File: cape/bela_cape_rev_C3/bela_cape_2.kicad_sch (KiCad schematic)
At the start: 18 parts, among them IC7 TSV524xIQ4T, IC8 TSV524xIQ4T, IC9 ADS8168

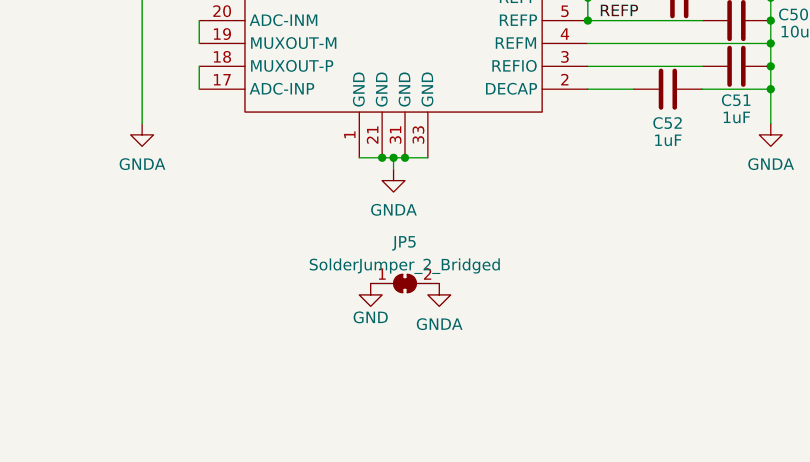
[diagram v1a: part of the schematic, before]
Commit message: removed sym-lib-table with a reference to an unused and obsolete local library
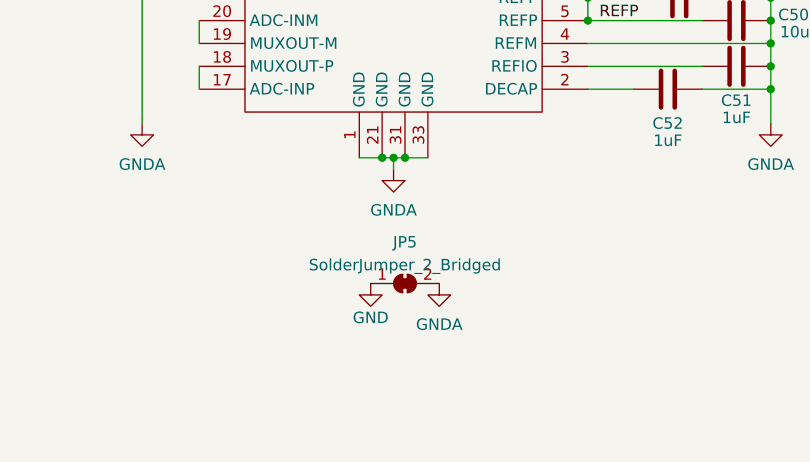
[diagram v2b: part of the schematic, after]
